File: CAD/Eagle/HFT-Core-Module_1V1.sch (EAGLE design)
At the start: 400 parts, among them Q0521 ABS07-32.768KHZ, Q0811 ABM03B-32.000MHZ, Q0911 ABM3B-16MHZ-10-R50-1-U, T1201 MMBT2222, T1202 MMBT2222, T1203 MMBT2222, U0111 STM32L4Z_144PIN_SMPS, U0431 PAM2305AAB120, U0601 LM4120IM5-3.0, U0611 MAX5217, U0631 CFPT-141-20MHZ, U0641 OPA354, U0701 Si5338, U0801 SX1276, U0901 AX5243, U0911 PE4259, U0921 PE4259, U0991 PE4259, U1101 MCP3911A0-E-SS, U1111 MAX5136AGTG+, U1121 OPA354, U1131 OPA354, U1141 OPA354, U1201 NHD-C0220BIZ_2X20CHARS, U1301 MPU-9250, U1311 MS5607-02BA03, U1321 SHT31-DIS, U1402 SPV1040T, U1501 TS5A23166, U1601 SC189ZSKTRT, U1701 TS5A23166, U1801 TS5A23166, U1901 TS5A23166, X1261 TTE_EN11-HSM, X1401 WIRE-TO-BOARD_5MM08_1X02, X2001 MOLEX 105017-0001, X2101 SMA_SMT_AMPHENOL-901-143, SAM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, X2111 SMA_SMT_AMPHENOL-901-143, SAM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, X2201 CUI SJ1-3535NS, X2211 CUI SJ1-3535NS, X2311 2X20/90_1MM27_HARWIN_M50-3202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, X2312 2X20/90_1MM27_HARWIN_M50-3202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, X2321 2X20/90_1MM27_HARWIN_M50-3202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, X2322 2X20/90_1MM27_HARWIN_M50-3202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, X2331 2X20/90_1MM27_HARWIN_M50-3202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, X2332 2X20/90_1MM27_HARWIN_M50-3202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

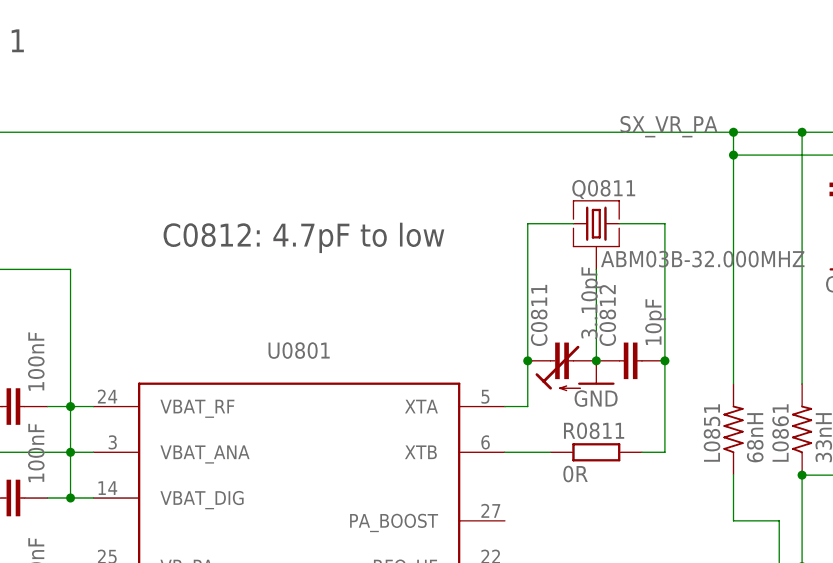
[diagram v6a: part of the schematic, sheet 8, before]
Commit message: HW_1V1 - SX1276 change of cap to 12pF
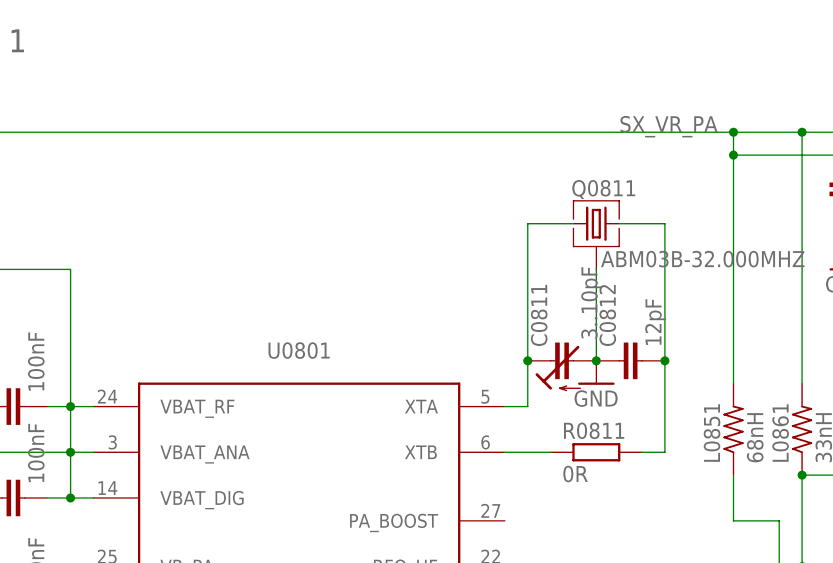
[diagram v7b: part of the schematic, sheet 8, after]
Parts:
- C0812: value 10pF -> 12pF
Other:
- note removed: "C0812: 4.7pF to low"
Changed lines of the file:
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@@
 <part name="GND0811" library="df4iah_supply" deviceset="GND" device=""/>
 <part name="C0811" library="df4iah_c-trimm" deviceset="C-TRIMM" device="3MM2_2MM5" value="3..10pF"/>
-<part name="C0812" library="rcl" deviceset="C-EU" device="C0603" value="10pF"/>
+<part name="C0812" library="rcl" deviceset="C-EU" device="C0603" value="12pF"/>
 <part name="C0806" library="rcl" deviceset="C-EU" device="C0603" value="100nF"/>
 <part name="C0807" library="rcl" deviceset="C-EU" device="C0603" value="100nF"/>
@@
 <text x="88.9" y="33.02" size="1.778" layer="97">to be replaced by:
 SX1262</text>
-<text x="86.36" y="144.78" size="2.54" layer="97">C0812: 4.7pF to low</text>
 </plain>
 <instances>

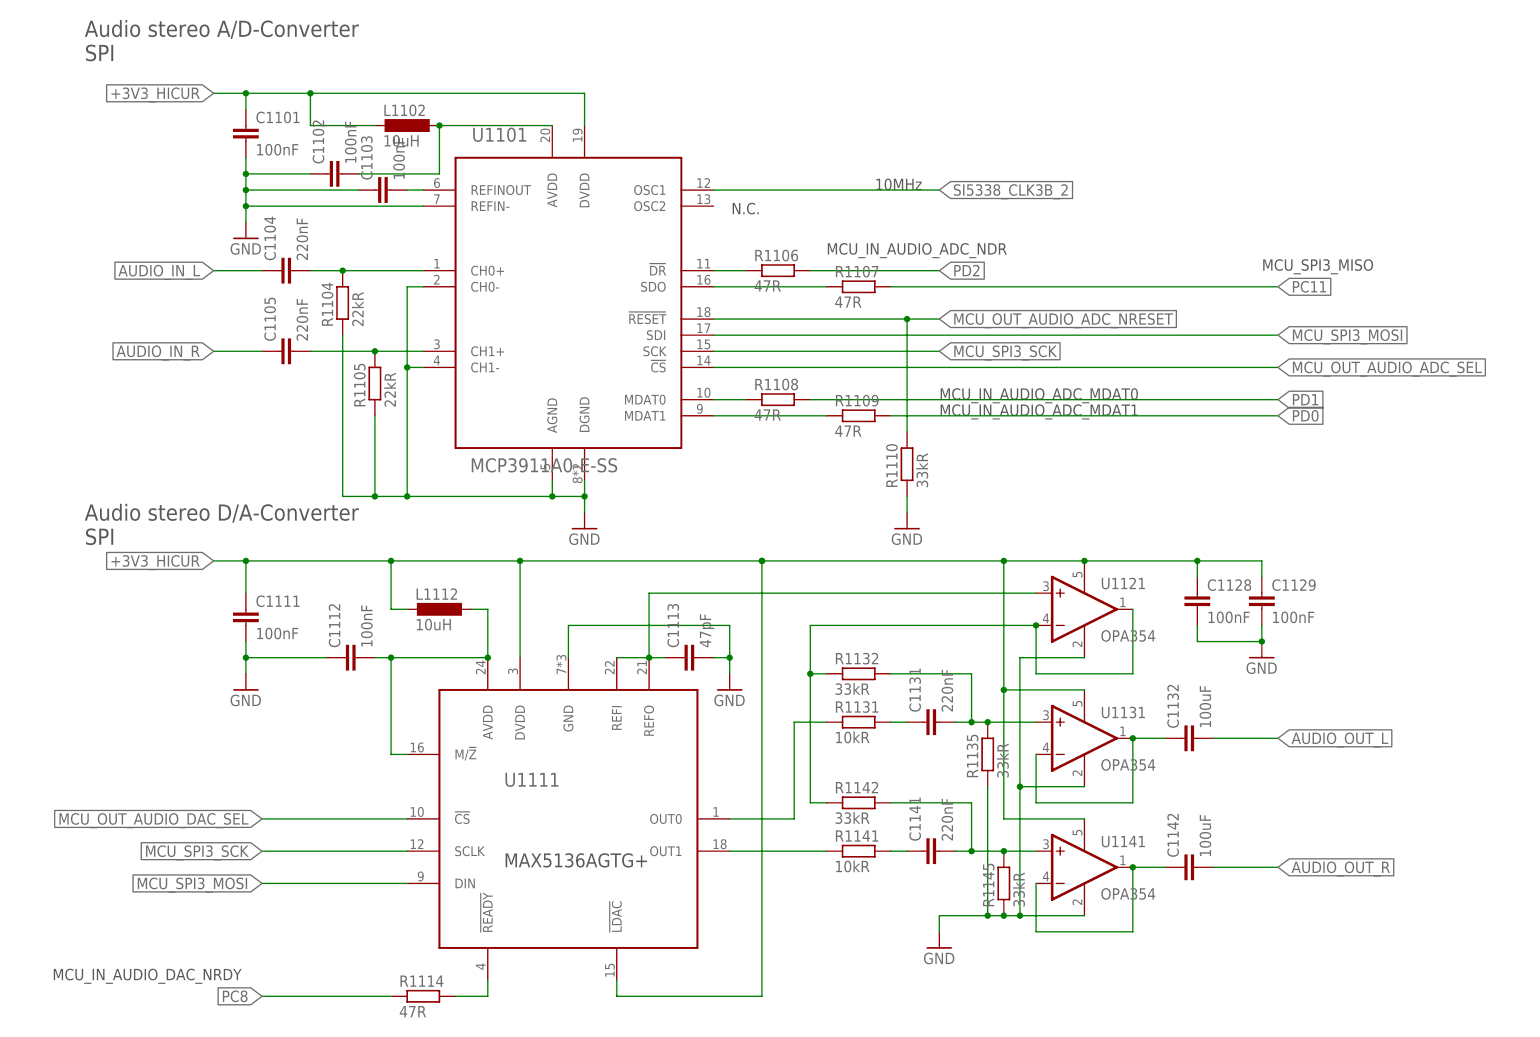
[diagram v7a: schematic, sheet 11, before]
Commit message: HW_1V1 - AUDIO ADC and DAC - replaced by I2S streaming devices
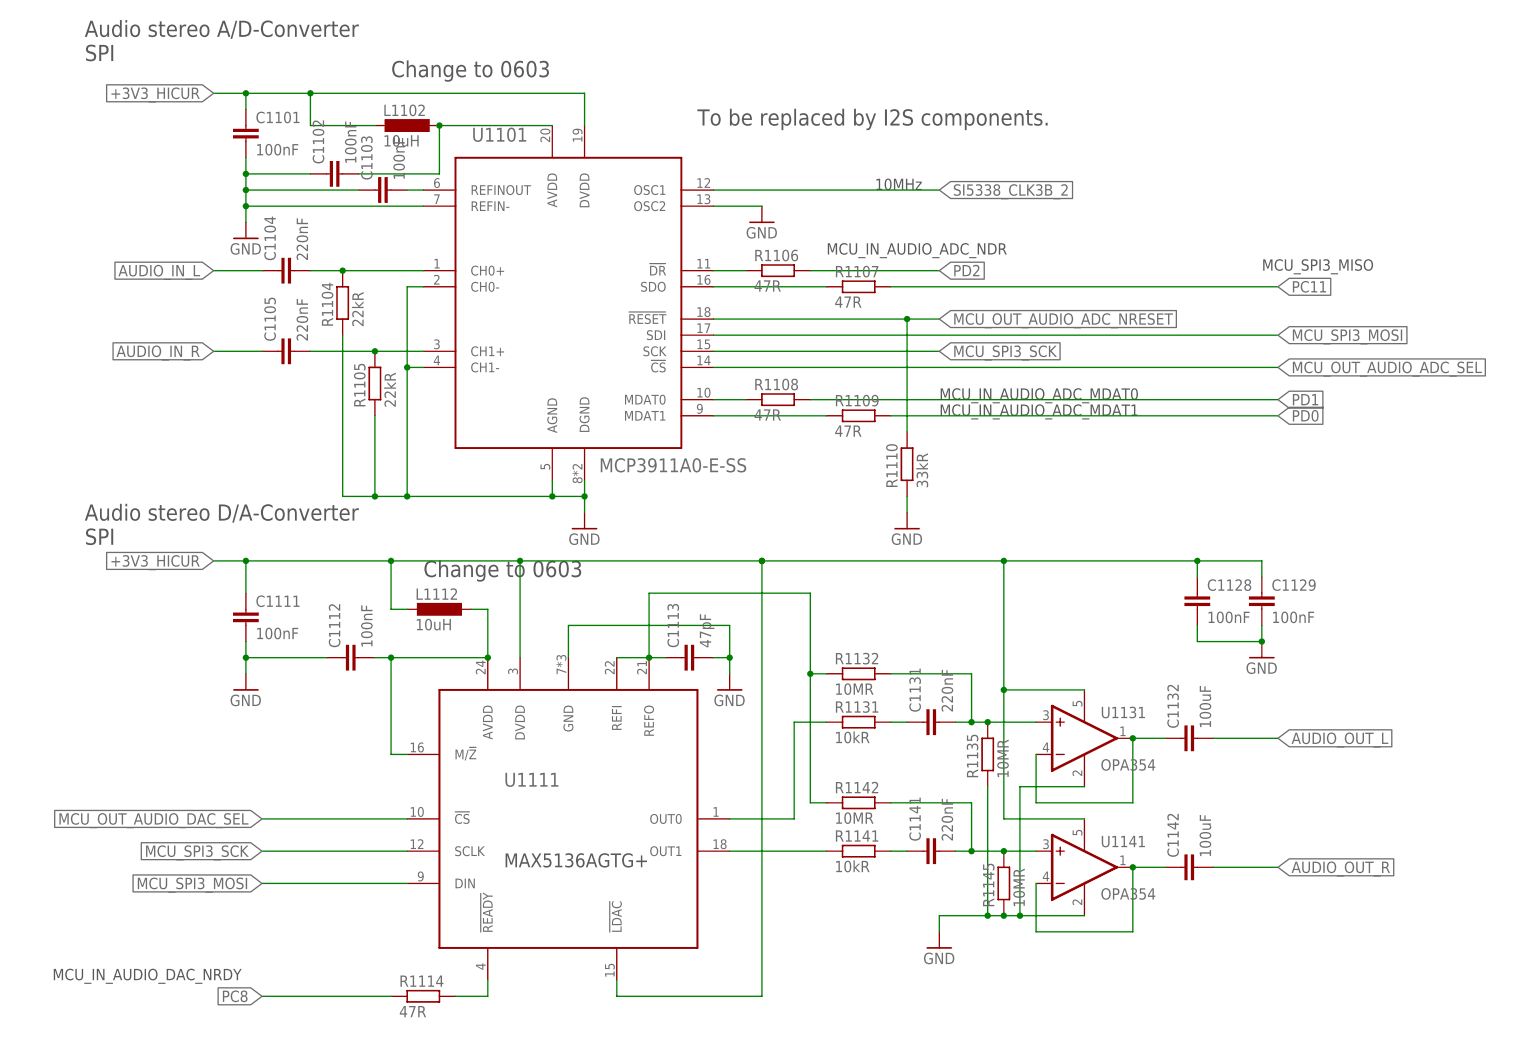
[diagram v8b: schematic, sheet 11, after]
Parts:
- removed U1121: OPA354, df4iah_opamp:OPA354
- R1132, R1135, R1142, R1145: value 33kR -> 10MR
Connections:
- net MCU_SX_TX_RX_CTRL renamed MCU_OUT_SX_HF_!LF!_CTRL
- net SX_RXTX_2 renamed SX_TX_!RX!_CTRL
- removed net MAX5136_REF_OP: R1132.1, R1142.1, U1121.-IN, U1121.OUT
- net +3V3_HICUR: no longer U1121.V+
- net GND: now also U1101.OSC2; no longer U1121.V-
- net MAX5136_REF: now also R1132.1, R1142.1; no longer U1121.+IN
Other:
- note added: "Change to 0603"
- note added: "TX: high / RX: low"
- note added: "To be replaced by I2S components."
- note removed: "N.C."
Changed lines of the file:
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@@
 <part name="C1112" library="rcl" deviceset="C-EU" device="C0603" value="100nF"/>
 <part name="R1114" library="rcl" deviceset="R-EU_" device="R0603" value="47R"/>
-<part name="R1132" library="rcl" deviceset="R-EU_" device="R0603" value="33kR"/>
-<part name="R1142" library="rcl" deviceset="R-EU_" device="R0603" value="33kR"/>
+<part name="R1132" library="rcl" deviceset="R-EU_" device="R0603" value="10MR"/>
+<part name="R1142" library="rcl" deviceset="R-EU_" device="R0603" value="10MR"/>
 <part name="R1131" library="rcl" deviceset="R-EU_" device="R0603" value="10kR"/>
 <part name="R1141" library="rcl" deviceset="R-EU_" device="R0603" value="10kR"/>
-<part name="U1121" library="df4iah_opamp" deviceset="OPA354" device=""/>
 <part name="U1131" library="df4iah_opamp" deviceset="OPA354" device=""/>
 <part name="U1141" library="df4iah_opamp" deviceset="OPA354" device=""/>
@@
 <part name="C1131" library="df4iah_rcl" deviceset="C-EU" device="C0603" value="220nF"/>
 <part name="GND1121" library="df4iah_supply" deviceset="GND" device=""/>
-<part name="R1135" library="rcl" deviceset="R-EU_" device="R0603" value="33kR"/>
-<part name="R1145" library="rcl" deviceset="R-EU_" device="R0603" value="33kR"/>
+<part name="R1135" library="rcl" deviceset="R-EU_" device="R0603" value="10MR"/>
+<part name="R1145" library="rcl" deviceset="R-EU_" device="R0603" value="10MR"/>
 <part name="GND1102" library="df4iah_supply" deviceset="GND" device=""/>
 <part name="U1101" library="df4iah_adc" deviceset="MCP3911" device="" value="MCP3911A0-E-SS"/>
@@
 <part name="C0532" library="rcl" deviceset="C-EU" device="C0603" value="12pF"/>
 <part name="GND0532" library="df4iah_supply" deviceset="GND" device=""/>
+<part name="GND1104" library="df4iah_supply" deviceset="GND" device=""/>
 </parts>
 <sheets>
@@
 </segment>
 </net>
-<net name="MCU_SX_TX_RX_CTRL" class="0">
+<net name="MCU_OUT_SX_HF_!LF!_CTRL" class="0">
 <segment>
 <pinref part="R0277" gate="G$1" pin="2"/>
@@
 </segment>
 </net>
-<net name="SX_RXTX_2" class="0">
+<net name="SX_TX_!RX!_CTRL" class="0">
 <segment>
 <pinref part="R0801" gate="G$1" pin="2"/>
@@
 <plain>
 <text x="50.8" y="25.4" size="1.778" layer="97">HF: high / LF: low</text>
+<text x="50.8" y="86.36" size="1.778" layer="97">TX: high / RX: low</text>
 </plain>
 <instances>
@@
 </segment>
 </net>
-<net name="SX_RXTX_2" class="0">
-<segment>
-<wire x1="35.56" y1="88.9" x2="86.36" y2="88.9" width="0.1524" layer="91"/>
-<wire x1="86.36" y1="88.9" x2="86.36" y2="111.76" width="0.1524" layer="91"/>
-<pinref part="U0911" gate="G$1" pin="CTRL"/>
-<wire x1="86.36" y1="111.76" x2="81.28" y2="111.76" width="0.1524" layer="91"/>
-<wire x1="86.36" y1="88.9" x2="86.36" y2="43.18" width="0.1524" layer="91"/>
-<junction x="86.36" y="88.9"/>
-<pinref part="U0921" gate="G$1" pin="CTRL"/>
-<wire x1="86.36" y1="43.18" x2="81.28" y2="43.18" width="0.1524" layer="91"/>
-<label x="35.56" y="88.9" size="1.778" layer="95" rot="R180" xref="yes"/>
-</segment>
-</net>
 <net name="SX_HF_2" class="0">
 <segment>
@@
 </segment>
 </net>
-<net name="MCU_SX_TX_RX_CTRL" class="0">
+<net name="MCU_OUT_SX_HF_!LF!_CTRL" class="0">
 <segment>
 <pinref part="U0991" gate="G$1" pin="CTRL"/>
@@
 </segment>
 </net>
+<net name="SX_TX_!RX!_CTRL" class="0">
+<segment>
+<wire x1="35.56" y1="88.9" x2="86.36" y2="88.9" width="0.1524" layer="91"/>
+<wire x1="86.36" y1="88.9" x2="86.36" y2="111.76" width="0.1524" layer="91"/>
+<pinref part="U0911" gate="G$1" pin="CTRL"/>
+<wire x1="86.36" y1="111.76" x2="81.28" y2="111.76" width="0.1524" layer="91"/>
+<wire x1="86.36" y1="88.9" x2="86.36" y2="43.18" width="0.1524" layer="91"/>
+<junction x="86.36" y="88.9"/>
+<pinref part="U0921" gate="G$1" pin="CTRL"/>
+<wire x1="86.36" y1="43.18" x2="81.28" y2="43.18" width="0.1524" layer="91"/>
+<label x="35.56" y="88.9" size="1.778" layer="95" rot="R180" xref="yes"/>
+</segment>
+</net>
 </nets>
 </sheet>
@@
 <text x="22.86" y="162.56" size="2.54" layer="97" ratio="15">Audio stereo A/D-Converter
 SPI</text>
-<text x="124.714" y="138.43" size="1.778" layer="97">N.C.</text>
 <text x="147.32" y="142.24" size="1.778" layer="97">10MHz</text>
 <text x="22.86" y="86.36" size="2.54" layer="97" ratio="15">Audio stereo D/A-Converter
@@
 <text x="139.7" y="132.08" size="1.778" layer="97">MCU_IN_AUDIO_ADC_NDR</text>
 <text x="208.28" y="129.54" size="1.778" layer="97">MCU_SPI3_MISO</text>
+<text x="71.12" y="160.02" size="2.54" layer="97">Change to 0603</text>
+<text x="76.2" y="81.28" size="2.54" layer="97">Change to 0603</text>
+<text x="119.38" y="152.4" size="2.54" layer="97">To be replaced by I2S components.</text>
 </plain>
 <instances>
@@
 <instance part="R1131" gate="G$1" x="144.78" y="58.42"/>
 <instance part="R1141" gate="G$1" x="144.78" y="38.1"/>
-<instance part="U1121" gate="G$1" x="180.34" y="76.2"/>
 <instance part="U1131" gate="G$1" x="180.34" y="55.88"/>
 <instance part="U1141" gate="G$1" x="180.34" y="35.56"/>
@@
 <instance part="R1145" gate="G$1" x="167.64" y="33.02" rot="R90"/>
 <instance part="GND1102" gate="1" x="101.6" y="88.9"/>
-<instance part="U1101" gate="G$1" x="99.06" y="124.46"/>
+<instance part="U1101" gate="G$1" x="99.06" y="124.46" smashed="yes">
+<attribute name="NAME" x="83.82" y="149.86" size="2.1844" layer="95" ratio="10"/>
+<attribute name="VALUE" x="103.886" y="97.79" size="2.1844" layer="96" ratio="10"/>
+</instance>
 <instance part="R1106" gate="G$1" x="132.08" y="129.54"/>
 <instance part="R1107" gate="G$1" x="144.78" y="127"/>
@@
 <instance part="GND1122" gate="1" x="208.28" y="68.58"/>
 <instance part="C1128" gate="G$1" x="198.12" y="78.74"/>
+<instance part="GND1104" gate="1" x="129.54" y="137.16"/>
 </instances>
 <busses>
@@
 <wire x1="170.18" y1="48.26" x2="180.34" y2="48.26" width="0.1524" layer="91"/>
 <junction x="170.18" y="27.94"/>
-<wire x1="170.18" y1="48.26" x2="170.18" y2="68.58" width="0.1524" layer="91"/>
-<pinref part="U1121" gate="G$1" pin="V-"/>
-<wire x1="170.18" y1="68.58" x2="180.34" y2="68.58" width="0.1524" layer="91"/>
-<junction x="170.18" y="48.26"/>
 <pinref part="R1145" gate="G$1" pin="1"/>
 <pinref part="R1135" gate="G$1" pin="1"/>
@@
 <junction x="208.28" y="71.12"/>
 </segment>
-</net>
-<net name="MAX5136_REF" class="0">
 <segment>
-<pinref part="U1111" gate="G$1" pin="REFI"/>
-<wire x1="106.68" y1="68.58" x2="111.76" y2="68.58" width="0.1524" layer="91"/>
-<pinref part="U1111" gate="G$1" pin="REFO"/>
-<wire x1="111.76" y1="68.58" x2="114.3" y2="68.58" width="0.1524" layer="91"/>
-<junction x="111.76" y="68.58"/>
-<pinref part="C1113" gate="G$1" pin="1"/>
-<wire x1="111.76" y1="68.58" x2="111.76" y2="78.74" width="0.1524" layer="91"/>
-<pinref part="U1121" gate="G$1" pin="+IN"/>
-<wire x1="172.72" y1="78.74" x2="111.76" y2="78.74" width="0.1524" layer="91"/>
+<pinref part="GND1104" gate="1" pin="GND"/>
+<pinref part="U1101" gate="G$1" pin="OSC2"/>
+<wire x1="129.54" y1="139.7" x2="121.92" y2="139.7" width="0.1524" layer="91"/>
 </segment>
 </net>
@@
 <junction x="167.64" y="63.5"/>
 <pinref part="U1131" gate="G$1" pin="V+"/>
-<pinref part="U1121" gate="G$1" pin="V+"/>
-<wire x1="167.64" y1="83.82" x2="180.34" y2="83.82" width="0.1524" layer="91"/>
 <junction x="167.64" y="83.82"/>
 <pinref part="C1129" gate="G$1" pin="1"/>
-<wire x1="180.34" y1="83.82" x2="198.12" y2="83.82" width="0.1524" layer="91"/>
+<wire x1="167.64" y1="83.82" x2="198.12" y2="83.82" width="0.1524" layer="91"/>
 <wire x1="198.12" y1="83.82" x2="208.28" y2="83.82" width="0.1524" layer="91"/>
 <wire x1="208.28" y1="83.82" x2="208.28" y2="81.28" width="0.1524" layer="91"/>
@@
 <wire x1="198.12" y1="83.82" x2="198.12" y2="81.28" width="0.1524" layer="91"/>
 <junction x="198.12" y="83.82"/>
-<junction x="180.34" y="83.82"/>
 </segment>
 <segment>
@@
 </segment>
 </net>
-<net name="MAX5136_REF_OP" class="0">
-<segment>
-<pinref part="U1121" gate="G$1" pin="-IN"/>
-<wire x1="172.72" y1="73.66" x2="172.72" y2="66.04" width="0.1524" layer="91"/>
-<wire x1="172.72" y1="66.04" x2="187.96" y2="66.04" width="0.1524" layer="91"/>
-<pinref part="U1121" gate="G$1" pin="OUT"/>
-<wire x1="187.96" y1="66.04" x2="187.96" y2="76.2" width="0.1524" layer="91"/>
-<wire x1="172.72" y1="73.66" x2="137.16" y2="73.66" width="0.1524" layer="91"/>
-<wire x1="137.16" y1="73.66" x2="137.16" y2="66.04" width="0.1524" layer="91"/>
-<pinref part="R1142" gate="G$1" pin="1"/>
-<wire x1="137.16" y1="66.04" x2="137.16" y2="45.72" width="0.1524" layer="91"/>
-<wire x1="137.16" y1="45.72" x2="139.7" y2="45.72" width="0.1524" layer="91"/>
-<pinref part="R1132" gate="G$1" pin="1"/>
-<wire x1="137.16" y1="66.04" x2="139.7" y2="66.04" width="0.1524" layer="91"/>
-<junction x="137.16" y="66.04"/>
-<junction x="172.72" y="73.66"/>
-</segment>
-</net>
 <net name="MCU_OUT_AUDIO_ADC_NRESET" class="0">
 <segment>
@@
 </segment>
 </net>
+<net name="MAX5136_REF" class="0">
+<segment>
+<wire x1="137.16" y1="78.74" x2="137.16" y2="66.04" width="0.1524" layer="91"/>
+<pinref part="R1142" gate="G$1" pin="1"/>
+<wire x1="137.16" y1="66.04" x2="137.16" y2="45.72" width="0.1524" layer="91"/>
+<wire x1="137.16" y1="45.72" x2="139.7" y2="45.72" width="0.1524" layer="91"/>
+<pinref part="R1132" gate="G$1" pin="1"/>
+<wire x1="137.16" y1="66.04" x2="139.7" y2="66.04" width="0.1524" layer="91"/>
+<junction x="137.16" y="66.04"/>
+<pinref part="U1111" gate="G$1" pin="REFI"/>
+<wire x1="106.68" y1="68.58" x2="111.76" y2="68.58" width="0.1524" layer="91"/>
+<pinref part="U1111" gate="G$1" pin="REFO"/>
+<wire x1="111.76" y1="68.58" x2="114.3" y2="68.58" width="0.1524" layer="91"/>
+<junction x="111.76" y="68.58"/>
+<pinref part="C1113" gate="G$1" pin="1"/>
+<wire x1="111.76" y1="68.58" x2="111.76" y2="78.74" width="0.1524" layer="91"/>
+<wire x1="137.16" y1="78.74" x2="111.76" y2="78.74" width="0.1524" layer="91"/>
+</segment>
+</net>
